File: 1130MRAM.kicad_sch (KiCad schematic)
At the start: 117 parts, among them J1 Screw_Terminal_01x03, J1A09 SLTpad, J1A11 SLTpad, K1E09 SLTpad, K1E11 SLTpad, M1A09 SLTpad, M1A11 SLTpad, M1C09 SLTpad, M1D09 SLTpad, M1E09 SLTpad, M1E11 SLTpad, SW1 SLTpad, U1 MR0A16AYS35, U10 74LS03, U11 74LS03, U12 SN74LVC1G123DCUR, U13 SN74LVC1G123DCUR, U14 74LS00, U15 74LS86, U16 74LS86, U17 74LS86, U18 74LS86, U2 SN74LV240APWR, U3 SN74LV240APWR, U5 SN74LVC1G123DCUR, U6 SN74LVC1G123DCUR, U7 74LS03, U8 74LS03, U9 74LS03

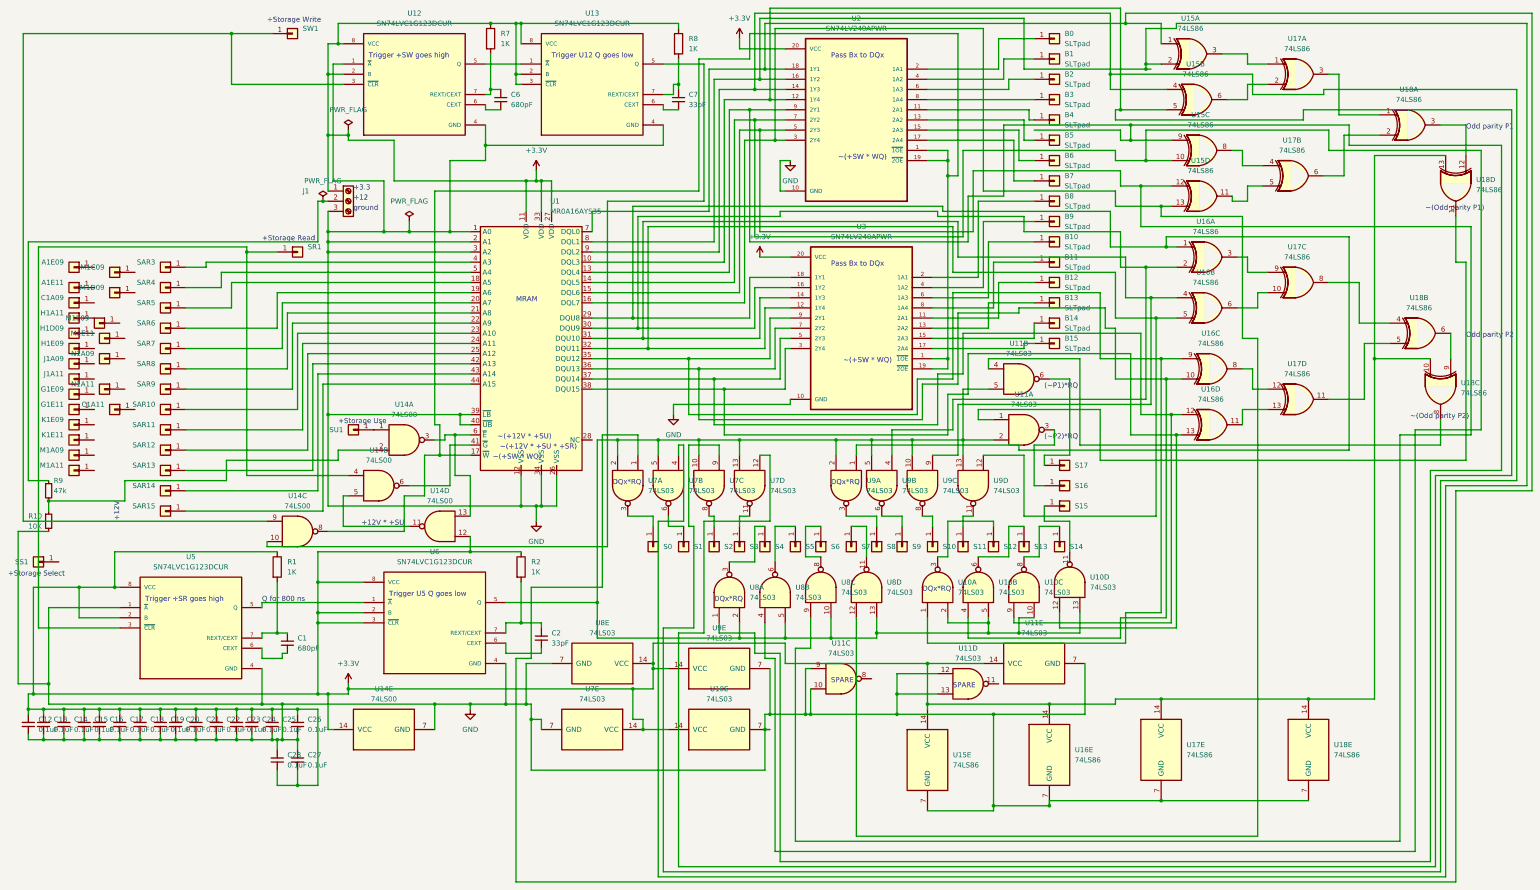
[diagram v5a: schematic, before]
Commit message: Post debugging version
Handles duplicate pins on cables T1, T3 and T4 that are only bridged on the IBM SLT backplane we are replacing with this board. Gets control, address, data and sense signals to the circuitry on the PCB.
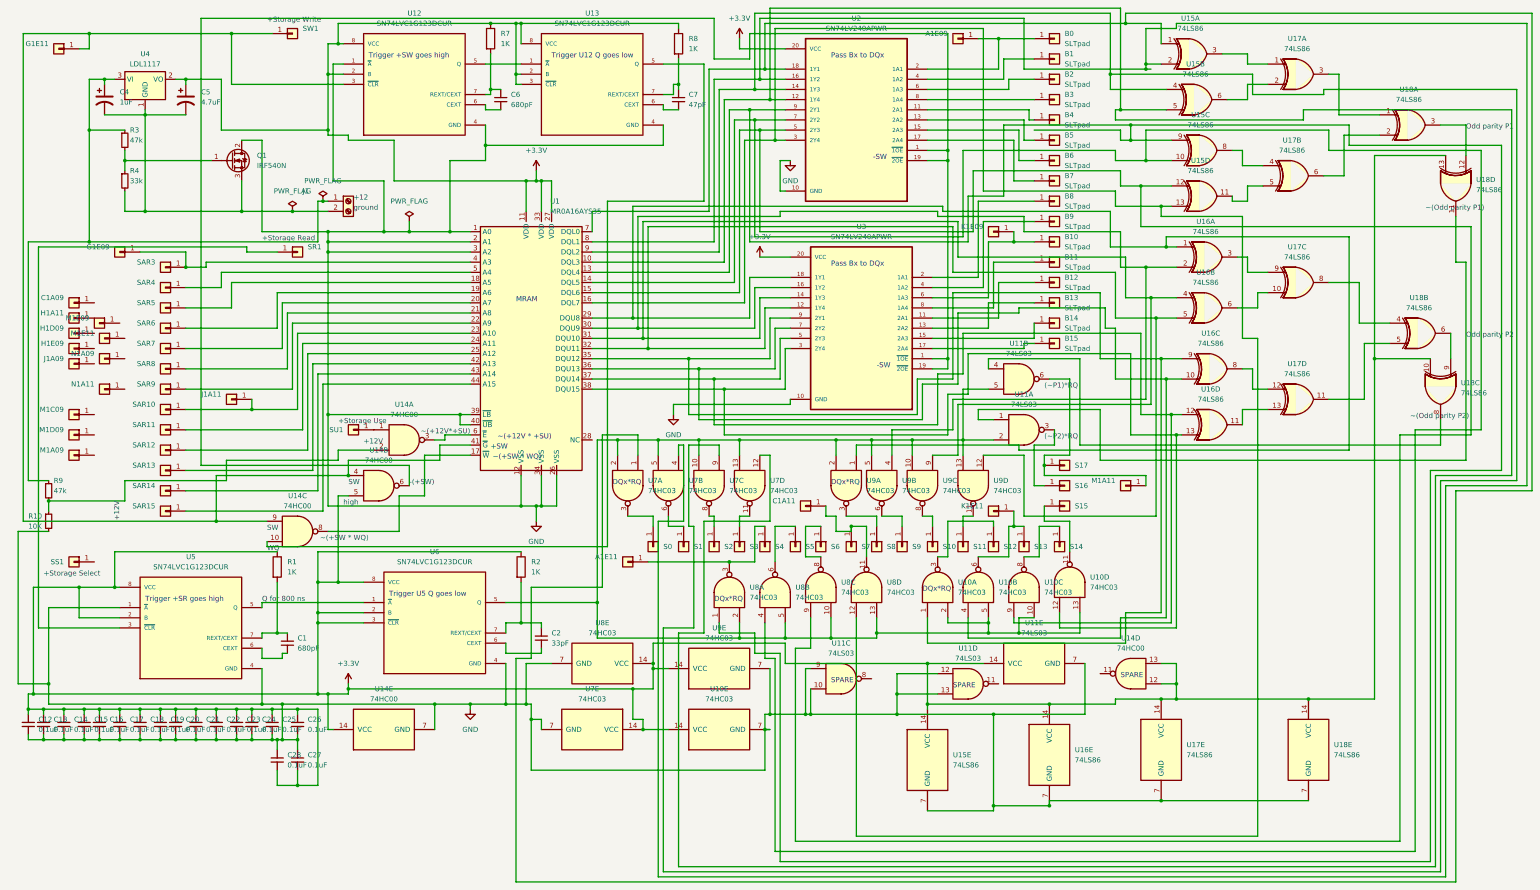
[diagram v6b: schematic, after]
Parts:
- added C4: 1uF, Capacitor_SMD:C_0805_2012Metric, symbol Device:C_Polarized_US
- added C5: 4.7uF, Capacitor_SMD:C_0805_2012Metric, symbol Device:C_Polarized_US
- added Q1: IRF540N, Package_TO_SOT_SMD:TO-263-2, symbol Transistor_FET:IRF540N
- added R3: 47k, Resistor_SMD:R_0805_2012Metric, symbol Device:R_Small
- added R4: 33k, Resistor_SMD:R_0805_2012Metric, symbol Device:R_Small
- added U4: LDL1117, Package_TO_SOT_SMD:SOT-223-3_TabPin2, symbol Regulator_Linear:LD1117S18TR_SOT223
- C7: value 33pF -> 47pF
- J1: footprint Connector_Phoenix_MC_HighVoltage:PhoenixContact_MCV_1,5_3-G-5.08_1x03_P5.08mm_Vertical -> Connector_Phoenix_MC_HighVoltage:PhoenixContact_MCV_1,5_2-G-5.08_1x02_P5.08mm_Vertical; symbol Connector:Screw_Terminal_01x03 -> Connector:Screw_Terminal_01x02
- U10, U7, U8, U9: value 74LS03 -> 74HC03
- U14: value 74LS00 -> 74HC00
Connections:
- net +3.3V: now also U14.13, U14.5, C5.1, U4.2 (VO); no longer J1.1 (Pin_1)
- net GND: now also Q1.2 (D); no longer J1.3 (Pin_3)
- net at B10.1 (Pin_1), U3.6 (1A3): now also K1E09.1 (Pin_1)
- net at U1.6 (~{E}), U14.3: no longer U14.13
- net at S13.1 (Pin_1), U10.6: now also K1E11.1 (Pin_1)
- net at G1E09.1 (Pin_1): now also SAR3.1 (Pin_1), U1.4 (A3)
- net at SR1.1 (Pin_1), U5.3 (~{CLR}): no longer U14.4
- net at S7.1 (Pin_1), U8.11: now also C1A11.1 (Pin_1)
- net at S17.1 (Pin_1), U11.6: now also M1A11.1 (Pin_1)
- net at SAR10.1 (Pin_1), U1.23 (A10): now also J1A11.1 (Pin_1)
- net at S4.1 (Pin_1), U8.3: now also A1E11.1 (Pin_1)
- net at SW1.1 (Pin_1), U12.3 (~{CLR}), U14.9: now also G1E11.1 (Pin_1), U1.41 (~{G}), U14.4
- net at J1.2 (Pin_2): now also C4.2, C5.2, Q1.3 (S), R4.2, U4.1 (GND); no longer R9.1
- net at U2.1 (~{1OE}), U2.19 (~{2OE}), U3.1 (~{1OE})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: now also U14.6; no longer U1.17 (~{W}), U14.8
- net at B0.1 (Pin_1), U2.2 (1A1): now also A1E09.1 (Pin_1)
- net at U14.11: no longer U14.5
- new net: C4.1, J1.1 (Pin_1), R3.1, R9.1, U4.3 (VI)
- new net: Q1.1 (G), R3.2, R4.1
- new net: U1.17 (~{W}), U14.8
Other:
- note added: "+SW"
- note added: "-(+SW)"
- note added: "-SW"
- note added: "SW"
- note added: "WQ"
- note added: "high"
- note added: "~(+12V*+SU)"
- note removed: "+12V * +SU"
- note removed: "+3.3"
- note removed: "~(+12V * +SU * +SR)"
- moved on the sheet: A1E09, A1E11, C1A11, G1E09, G1E11, J1A11, K1E09, K1E11, M1A11, M1C09, M1D09, SS1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

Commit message: Switch to 74LCX38 for better output drive
prior open drain gate had insufficent current sink capacity to set the 1130's B register flipflop
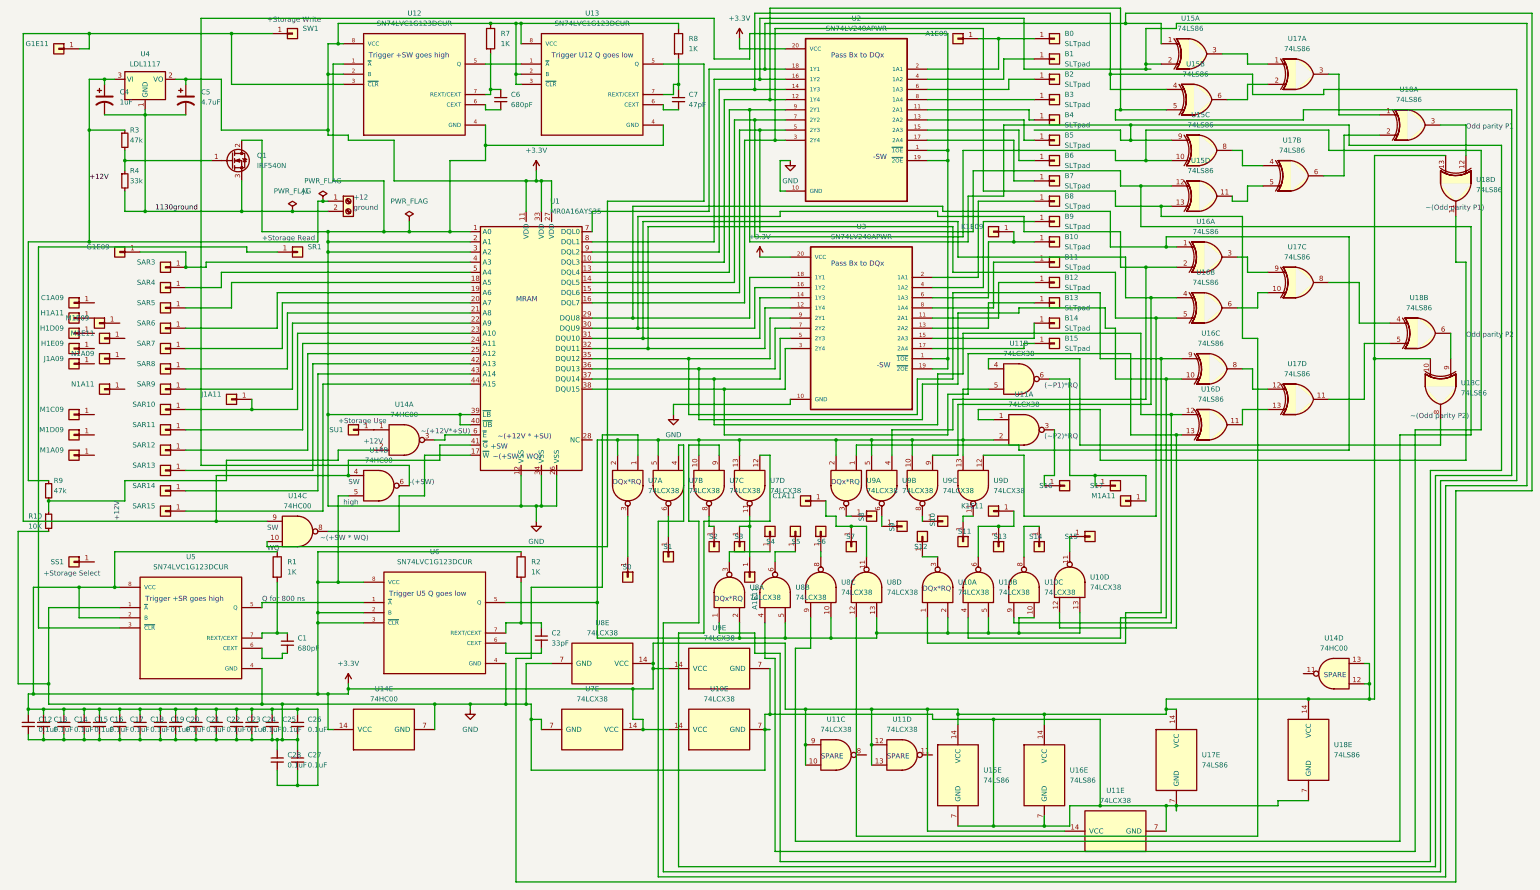
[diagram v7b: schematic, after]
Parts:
- U10, U7, U8, U9: value 74HC03 -> 74LCX38; footprint 1130MRAM:sn74lc03dr -> Package_SO:TSSOP-14_4.4x5mm_P0.65mm; symbol 1130mram:74LS03 -> 74xx:74LS03
- U11: value 74LS03 -> 74LCX38; footprint 1130MRAM:sn74lc03dr -> Package_SO:TSSOP-14_4.4x5mm_P0.65mm; symbol 1130mram:74LS03 -> 74xx:74LS03
- U14: symbol 74xx:74LS00 -> 74xx:74HC00
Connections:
- net +3.3V: now also U11.10, U11.12, U11.13, U11.9
- net GND: no longer U11.10, U11.12, U11.13, U11.9
- net at S4.1 (Pin_1), U8.3: no longer A1E11.1 (Pin_1)
- net 1130ground: now reaches C4.2, C5.2, J1.2 (Pin_2), Q1.3 (S), R4.2, U4.1 (GND)
- net +12V: now reaches C4.1, J1.1 (Pin_1), R3.1, R9.1, U4.3 (VI)
- net at S3.1 (Pin_1), U7.11: now also A1E11.1 (Pin_1)
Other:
- moved on the sheet: A1E11, C1A11, M1A11, S0, S1, S10, S11, S12, S13, S14, S15, S17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

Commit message: Corrected defect in design
Prior design optimization led to a failure mode that is experienced on the IBM 1130. Corrected the issue.
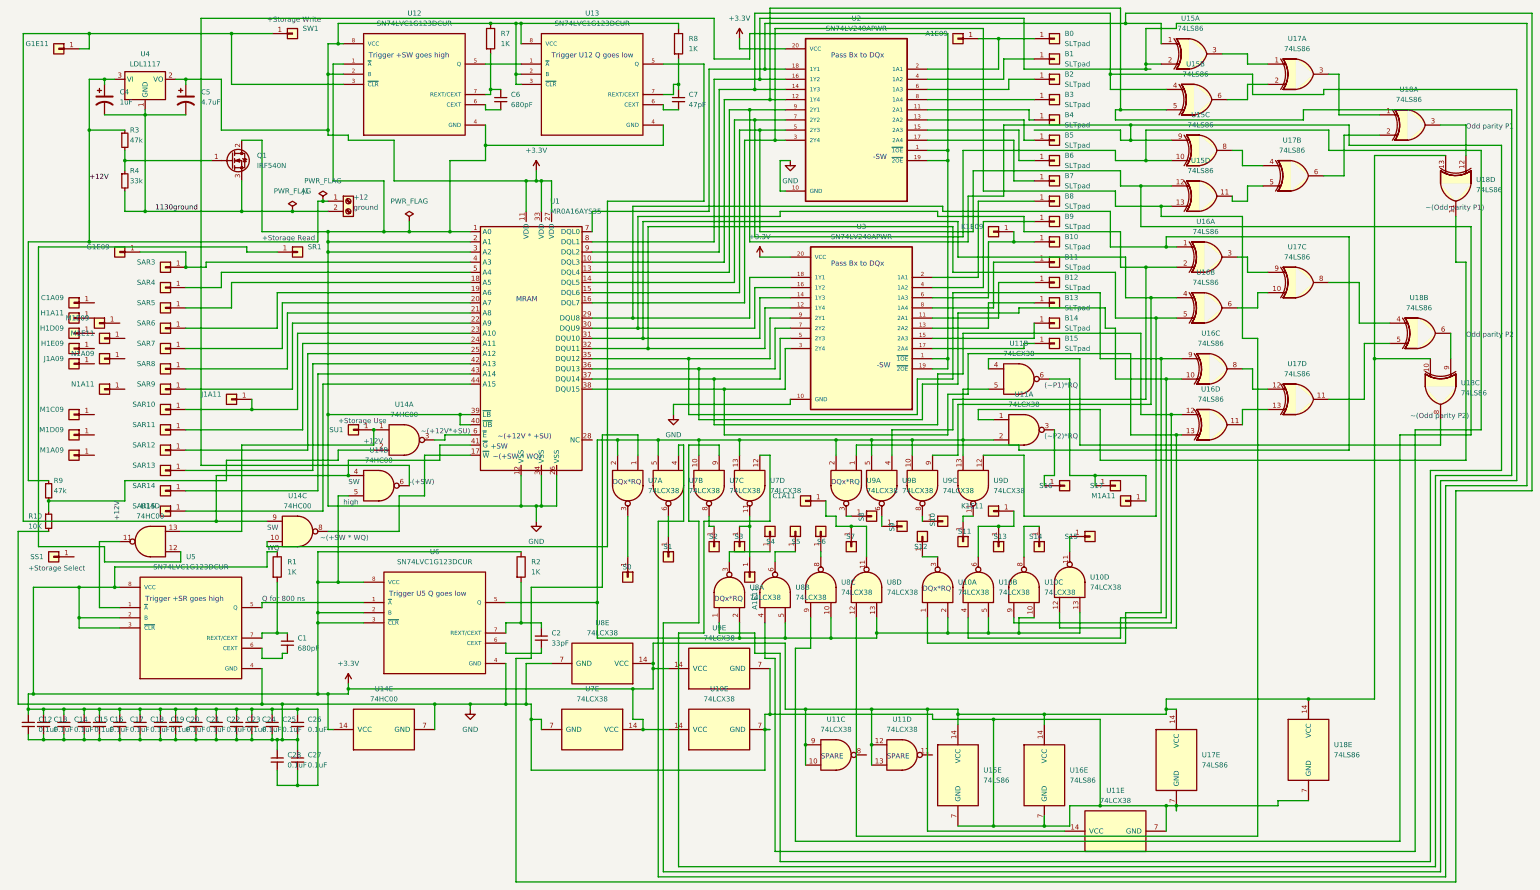
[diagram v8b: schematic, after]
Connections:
- net +3.3V: now also U5.3 (~{CLR}); no longer U14.12, U14.13
- net GND: no longer U5.1 (~{A})
- net at SU1.1 (Pin_1), U14.1: now also U14.13
- net at SR1.1 (Pin_1): now also U14.12; no longer U5.3 (~{CLR})
- net at U14.11: now also U5.1 (~{A})
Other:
- moved on the sheet: SS1, U14D
